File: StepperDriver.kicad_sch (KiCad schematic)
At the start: 13 parts, among them U5 A4988SETTR-T

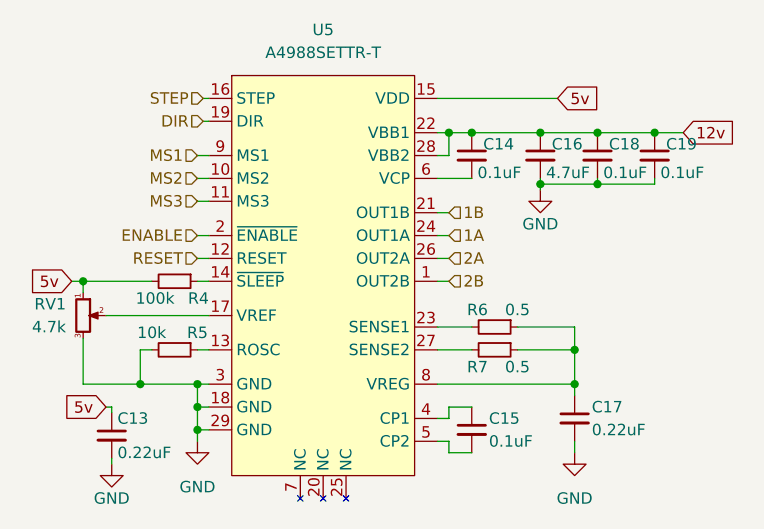
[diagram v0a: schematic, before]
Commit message: Added part numbers to majority of components
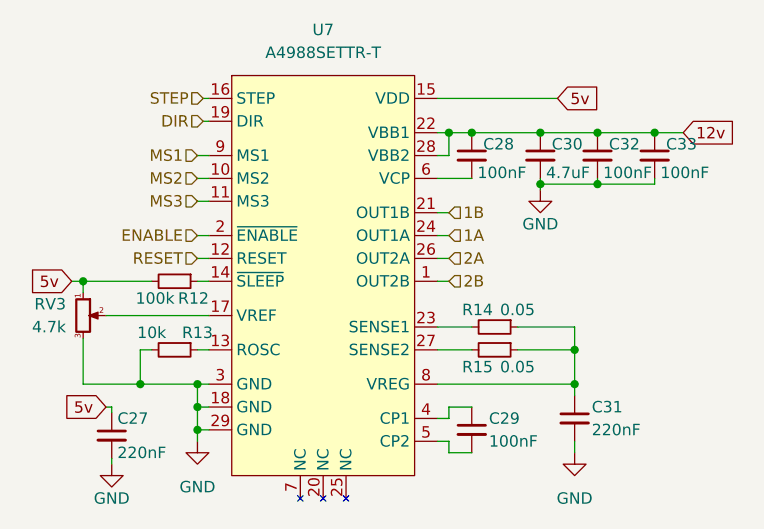
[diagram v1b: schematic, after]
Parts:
- C27: renamed from C13; value 0.22uF -> 220nF; footprint (none) -> Capacitor_SMD:C_0603_1608Metric; LSCS Part Number (none) -> C21120; Manufacturer Part Number (none) -> CL10B224KA8NNNC
- C28: renamed from C14; value 0.1uF -> 100nF; footprint (none) -> Capacitor_SMD:C_0603_1608Metric; LSCS Part Number (none) -> C1591; Manufacturer Part Number (none) -> CL10B104KB8NNNC
- C29: renamed from C15; value 0.1uF -> 100nF; footprint (none) -> Capacitor_SMD:C_0603_1608Metric; LSCS Part Number (none) -> C1591; Manufacturer Part Number (none) -> CL10B104KB8NNNC
- C30: renamed from C16; footprint (none) -> Capacitor_SMD:C_0603_1608Metric; LSCS Part Number (none) -> C69335; Manufacturer Part Number (none) -> CL10A475KA8NQNC
- C31: renamed from C17; value 0.22uF -> 220nF; footprint (none) -> Capacitor_SMD:C_0603_1608Metric; LSCS Part Number (none) -> C21120; Manufacturer Part Number (none) -> CL10B224KA8NNNC
- C32: renamed from C18; value 0.1uF -> 100nF; footprint (none) -> Capacitor_SMD:C_0603_1608Metric; LSCS Part Number (none) -> C1591; Manufacturer Part Number (none) -> CL10B104KB8NNNC
- C33: renamed from C19; value 0.1uF -> 100nF; footprint (none) -> Capacitor_SMD:C_0603_1608Metric; LSCS Part Number (none) -> C1591; Manufacturer Part Number (none) -> CL10B104KB8NNNC
- R12: renamed from R4; footprint (none) -> Resistor_SMD:R_0603_1608Metric; LSCS Part Number (none) -> C14675; Manufacturer Part Number (none) -> RC0603FR-07100KL
- R13: renamed from R5; footprint (none) -> Resistor_SMD:R_0603_1608Metric; LSCS Part Number (none) -> C25804; Manufacturer Part Number (none) -> 0603WAF1002T5E
- R14: renamed from R6; value 0.5 -> 0.05; footprint (none) -> Resistor_SMD:R_0603_1608Metric; LSCS Part Number (none) -> C158895; Manufacturer Part Number (none) -> RTT03R050FTP
- R15: renamed from R7; value 0.5 -> 0.05; footprint (none) -> Resistor_SMD:R_0603_1608Metric; LSCS Part Number (none) -> C158895; Manufacturer Part Number (none) -> RTT03R050FTP
- RV3: renamed from RV1; Manufacturer Part Number (none) -> VG039NCHXTB472
- U7: renamed from U5; Manufacturer Part Number (none) -> A4988SETTR-T

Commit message: Started assigning footprints
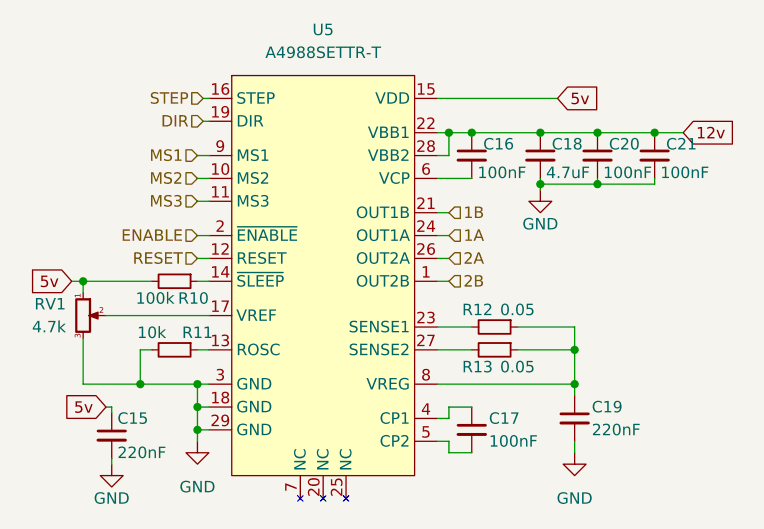
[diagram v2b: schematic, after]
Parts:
- U5: renamed from U7; footprint (none) -> Package_DFN_QFN:QFN-28-1EP_5x5mm_P0.5mm_EP3.35x3.35mm_ThermalVias
- renumbered C27 to C15, C28 to C16, C29 to C17, C30 to C18, C31 to C19, C32 to C20, C33 to C21, R12 to R10, R13 to R11, R14 to R12, R15 to R13, RV3 to RV1
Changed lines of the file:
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@@
   (symbol (lib_id "Device:R_Small") (at 159.385 97.79 270)
     (in_bom yes) (on_board yes)
-    (property "Reference" "R15" (id 0) (at 157.48 99.695 90))
+    (property "Reference" "R13" (id 0) (at 157.48 99.695 90))
     (property "Value" "0.05" (id 1) (at 161.925 99.695 90))
     (property "Footprint" "Resistor_SMD:R_0603_1608Metric" (id 2) (at 159.385 97.79 0)
@@
   (symbol (lib_id "Device:C_Small") (at 164.465 76.2 0)
     (in_bom yes) (on_board yes)
-    (property "Reference" "C30" (id 0) (at 165.735 74.9362 0)
+    (property "Reference" "C18" (id 0) (at 165.735 74.9362 0)
       (effects (font (size 1.27 1.27)) (justify left))
     )
@@
   (symbol (lib_id "power:GND") (at 168.275 109.22 0)
     (in_bom yes) (on_board yes) (fields_autoplaced)
-    (property "Reference" "#PWR021" (id 0) (at 168.275 115.57 0)
+    (property "Reference" "#PWR025" (id 0) (at 168.275 115.57 0)
       (effects (font (size 1.27 1.27)) hide)
     )
@@
   (symbol (lib_id "Device:R_Potentiometer_Small") (at 113.665 93.98 0)
     (in_bom yes) (on_board yes)
-    (property "Reference" "RV3" (id 0) (at 111.76 92.7099 0)
+    (property "Reference" "RV1" (id 0) (at 111.76 92.7099 0)
       (effects (font (size 1.27 1.27)) (justify right))
     )
@@
   (symbol (lib_id "Device:C_Small") (at 116.84 107.315 0)
     (in_bom yes) (on_board yes)
-    (property "Reference" "C27" (id 0) (at 117.475 105.4162 0)
+    (property "Reference" "C15" (id 0) (at 117.475 105.4162 0)
       (effects (font (size 1.27 1.27)) (justify left))
     )
@@
   (symbol (lib_id "power:GND") (at 116.84 110.49 0)
     (in_bom yes) (on_board yes)
-    (property "Reference" "#PWR018" (id 0) (at 116.84 116.84 0)
+    (property "Reference" "#PWR022" (id 0) (at 116.84 116.84 0)
       (effects (font (size 1.27 1.27)) hide)
     )
@@
   (symbol (lib_name "A4988SETTR-T_1") (lib_id "MotorBoard:A4988SETTR-T") (at 130.175 67.31 0)
     (in_bom yes) (on_board yes) (fields_autoplaced)
-    (property "Reference" "U7" (id 0) (at 140.335 62.23 0))
+    (property "Reference" "U5" (id 0) (at 140.335 62.23 0))
     (property "Value" "A4988SETTR-T" (id 1) (at 140.335 64.77 0))
-    (property "Footprint" "" (id 2) (at 165.735 68.58 0)
+    (property "Footprint" "Package_DFN_QFN:QFN-28-1EP_5x5mm_P0.5mm_EP3.35x3.35mm_ThermalVias" (id 2) (at 165.735 68.58 0)
       (effects (font (size 1.27 1.27)) hide)
     )
@@
   (symbol (lib_id "Device:C_Small") (at 156.845 76.2 0)
     (in_bom yes) (on_board yes)
-    (property "Reference" "C28" (id 0) (at 158.115 74.9362 0)
+    (property "Reference" "C16" (id 0) (at 158.115 74.9362 0)
       (effects (font (size 1.27 1.27)) (justify left))
     )
@@
   (symbol (lib_id "Device:R_Small") (at 159.385 95.25 270)
     (in_bom yes) (on_board yes)
-    (property "Reference" "R14" (id 0) (at 157.48 93.345 90))
+    (property "Reference" "R12" (id 0) (at 157.48 93.345 90))
     (property "Value" "0.05" (id 1) (at 161.925 93.345 90))
     (property "Footprint" "Resistor_SMD:R_0603_1608Metric" (id 2) (at 159.385 95.25 0)
@@
   (symbol (lib_id "Device:R_Small") (at 123.825 90.17 270)
     (in_bom yes) (on_board yes)
-    (property "Reference" "R12" (id 0) (at 127.6349 92.075 90)
+    (property "Reference" "R10" (id 0) (at 127.6349 92.075 90)
       (effects (font (size 1.27 1.27)) (justify right))
     )
@@
   (symbol (lib_id "Device:C_Small") (at 170.815 76.2 0)
     (in_bom yes) (on_board yes)
-    (property "Reference" "C32" (id 0) (at 172.085 74.9362 0)
+    (property "Reference" "C20" (id 0) (at 172.085 74.9362 0)
       (effects (font (size 1.27 1.27)) (justify left))
     )
@@
   (symbol (lib_id "Device:C_Small") (at 177.165 76.2 0)
     (in_bom yes) (on_board yes)
-    (property "Reference" "C33" (id 0) (at 178.435 74.9362 0)
+    (property "Reference" "C21" (id 0) (at 178.435 74.9362 0)
       (effects (font (size 1.27 1.27)) (justify left))
     )
@@
   (symbol (lib_id "Device:C_Small") (at 168.275 105.41 0)
     (in_bom yes) (on_board yes)
-    (property "Reference" "C31" (id 0) (at 170.18 104.1462 0)
+    (property "Reference" "C19" (id 0) (at 170.18 104.1462 0)
       (effects (font (size 1.27 1.27)) (justify left))
     )
@@
   (symbol (lib_id "power:GND") (at 164.465 80.01 0)
     (in_bom yes) (on_board yes)
-    (property "Reference" "#PWR020" (id 0) (at 164.465 86.36 0)
+    (property "Reference" "#PWR024" (id 0) (at 164.465 86.36 0)
       (effects (font (size 1.27 1.27)) hide)
     )
@@
   (symbol (lib_id "Device:C_Small") (at 156.845 106.68 0)
     (in_bom yes) (on_board yes)
-    (property "Reference" "C29" (id 0) (at 158.75 105.4162 0)
+    (property "Reference" "C17" (id 0) (at 158.75 105.4162 0)
       (effects (font (size 1.27 1.27)) (justify left))
     )
@@
   (symbol (lib_id "Device:R_Small") (at 123.825 97.79 270)
     (in_bom yes) (on_board yes)
-    (property "Reference" "R13" (id 0) (at 126.365 95.885 90))
+    (property "Reference" "R11" (id 0) (at 126.365 95.885 90))
     (property "Value" "10k" (id 1) (at 121.285 95.885 90))
     (property "Footprint" "Resistor_SMD:R_0603_1608Metric" (id 2) (at 123.825 97.79 0)
@@
   (symbol (lib_id "power:GND") (at 126.365 107.95 0)
     (in_bom yes) (on_board yes) (fields_autoplaced)
-    (property "Reference" "#PWR019" (id 0) (at 126.365 114.3 0)
-      (effects (font (size 1.27 1.27)) hide)
-    )
+    (property "Reference" "#PWR023" (id 0) (at 126.365 114.3 0)
+      (effects (font (size 1.27 1.27)) hide)
+    )

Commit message: Added servo headers
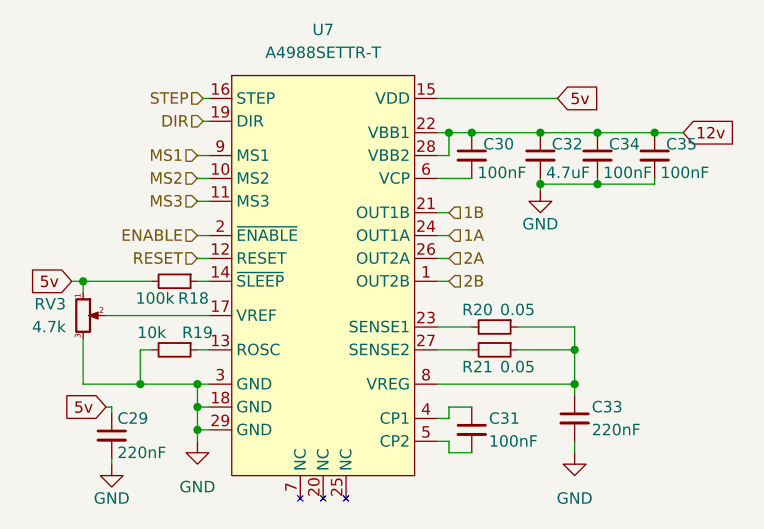
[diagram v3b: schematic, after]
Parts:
- RV3: renamed from RV1; footprint (none) -> MotorBoard:VG039NCHXTB472
- renumbered C15 to C29, C16 to C30, C17 to C31, C18 to C32, C19 to C33, C20 to C34, C21 to C35, R10 to R18, R11 to R19, R12 to R20, R13 to R21, U5 to U7
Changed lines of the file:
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@@
   (symbol (lib_id "Device:R_Small") (at 159.385 97.79 270)
     (in_bom yes) (on_board yes)
-    (property "Reference" "R13" (id 0) (at 157.48 99.695 90))
+    (property "Reference" "R21" (id 0) (at 157.48 99.695 90))
     (property "Value" "0.05" (id 1) (at 161.925 99.695 90))
     (property "Footprint" "Resistor_SMD:R_0603_1608Metric" (id 2) (at 159.385 97.79 0)
@@
   (symbol (lib_id "Device:C_Small") (at 164.465 76.2 0)
     (in_bom yes) (on_board yes)
-    (property "Reference" "C18" (id 0) (at 165.735 74.9362 0)
+    (property "Reference" "C32" (id 0) (at 165.735 74.9362 0)
       (effects (font (size 1.27 1.27)) (justify left))
     )
@@
   (symbol (lib_id "power:GND") (at 168.275 109.22 0)
     (in_bom yes) (on_board yes) (fields_autoplaced)
-    (property "Reference" "#PWR025" (id 0) (at 168.275 115.57 0)
+    (property "Reference" "#PWR033" (id 0) (at 168.275 115.57 0)
       (effects (font (size 1.27 1.27)) hide)
     )
@@
   (symbol (lib_id "Device:R_Potentiometer_Small") (at 113.665 93.98 0)
     (in_bom yes) (on_board yes)
-    (property "Reference" "RV1" (id 0) (at 111.76 92.7099 0)
+    (property "Reference" "RV3" (id 0) (at 111.76 92.7099 0)
       (effects (font (size 1.27 1.27)) (justify right))
     )
@@
       (effects (font (size 1.27 1.27)) (justify right))
     )
-    (property "Footprint" "" (id 2) (at 113.665 93.98 0)
+    (property "Footprint" "MotorBoard:VG039NCHXTB472" (id 2) (at 113.665 93.98 0)
       (effects (font (size 1.27 1.27)) hide)
     )
@@
   (symbol (lib_id "Device:C_Small") (at 116.84 107.315 0)
     (in_bom yes) (on_board yes)
-    (property "Reference" "C15" (id 0) (at 117.475 105.4162 0)
+    (property "Reference" "C29" (id 0) (at 117.475 105.4162 0)
       (effects (font (size 1.27 1.27)) (justify left))
     )
@@
   (symbol (lib_id "power:GND") (at 116.84 110.49 0)
     (in_bom yes) (on_board yes)
-    (property "Reference" "#PWR022" (id 0) (at 116.84 116.84 0)
+    (property "Reference" "#PWR030" (id 0) (at 116.84 116.84 0)
       (effects (font (size 1.27 1.27)) hide)
     )
@@
   (symbol (lib_name "A4988SETTR-T_1") (lib_id "MotorBoard:A4988SETTR-T") (at 130.175 67.31 0)
     (in_bom yes) (on_board yes) (fields_autoplaced)
-    (property "Reference" "U5" (id 0) (at 140.335 62.23 0))
+    (property "Reference" "U7" (id 0) (at 140.335 62.23 0))
     (property "Value" "A4988SETTR-T" (id 1) (at 140.335 64.77 0))
     (property "Footprint" "Package_DFN_QFN:QFN-28-1EP_5x5mm_P0.5mm_EP3.35x3.35mm_ThermalVias" (id 2) (at 165.735 68.58 0)
@@
   (symbol (lib_id "Device:C_Small") (at 156.845 76.2 0)
     (in_bom yes) (on_board yes)
-    (property "Reference" "C16" (id 0) (at 158.115 74.9362 0)
+    (property "Reference" "C30" (id 0) (at 158.115 74.9362 0)
       (effects (font (size 1.27 1.27)) (justify left))
     )
@@
   (symbol (lib_id "Device:R_Small") (at 159.385 95.25 270)
     (in_bom yes) (on_board yes)
-    (property "Reference" "R12" (id 0) (at 157.48 93.345 90))
+    (property "Reference" "R20" (id 0) (at 157.48 93.345 90))
     (property "Value" "0.05" (id 1) (at 161.925 93.345 90))
     (property "Footprint" "Resistor_SMD:R_0603_1608Metric" (id 2) (at 159.385 95.25 0)
@@
   (symbol (lib_id "Device:R_Small") (at 123.825 90.17 270)
     (in_bom yes) (on_board yes)
-    (property "Reference" "R10" (id 0) (at 127.6349 92.075 90)
+    (property "Reference" "R18" (id 0) (at 127.6349 92.075 90)
       (effects (font (size 1.27 1.27)) (justify right))
     )
@@
   (symbol (lib_id "Device:C_Small") (at 170.815 76.2 0)
     (in_bom yes) (on_board yes)
-    (property "Reference" "C20" (id 0) (at 172.085 74.9362 0)
+    (property "Reference" "C34" (id 0) (at 172.085 74.9362 0)
       (effects (font (size 1.27 1.27)) (justify left))
     )
@@
   (symbol (lib_id "Device:C_Small") (at 177.165 76.2 0)
     (in_bom yes) (on_board yes)
-    (property "Reference" "C21" (id 0) (at 178.435 74.9362 0)
+    (property "Reference" "C35" (id 0) (at 178.435 74.9362 0)
       (effects (font (size 1.27 1.27)) (justify left))
     )
@@
   (symbol (lib_id "Device:C_Small") (at 168.275 105.41 0)
     (in_bom yes) (on_board yes)
-    (property "Reference" "C19" (id 0) (at 170.18 104.1462 0)
+    (property "Reference" "C33" (id 0) (at 170.18 104.1462 0)
       (effects (font (size 1.27 1.27)) (justify left))
     )
@@
   (symbol (lib_id "power:GND") (at 164.465 80.01 0)
     (in_bom yes) (on_board yes)
-    (property "Reference" "#PWR024" (id 0) (at 164.465 86.36 0)
+    (property "Reference" "#PWR032" (id 0) (at 164.465 86.36 0)
       (effects (font (size 1.27 1.27)) hide)
     )
@@
   (symbol (lib_id "Device:C_Small") (at 156.845 106.68 0)
     (in_bom yes) (on_board yes)
-    (property "Reference" "C17" (id 0) (at 158.75 105.4162 0)
+    (property "Reference" "C31" (id 0) (at 158.75 105.4162 0)
       (effects (font (size 1.27 1.27)) (justify left))
     )
@@
   (symbol (lib_id "Device:R_Small") (at 123.825 97.79 270)
     (in_bom yes) (on_board yes)
-    (property "Reference" "R11" (id 0) (at 126.365 95.885 90))
+    (property "Reference" "R19" (id 0) (at 126.365 95.885 90))
     (property "Value" "10k" (id 1) (at 121.285 95.885 90))
     (property "Footprint" "Resistor_SMD:R_0603_1608Metric" (id 2) (at 123.825 97.79 0)
@@
   (symbol (lib_id "power:GND") (at 126.365 107.95 0)
     (in_bom yes) (on_board yes) (fields_autoplaced)
-    (property "Reference" "#PWR023" (id 0) (at 126.365 114.3 0)
-      (effects (font (size 1.27 1.27)) hide)
-    )
+    (property "Reference" "#PWR031" (id 0) (at 126.365 114.3 0)
+      (effects (font (size 1.27 1.27)) hide)
+    )

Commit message: Began work on PCB layout
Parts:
- removed C33: 220nF, Capacitor_SMD:C_0603_1608Metric, symbol Device:C_Small
- added C19: 220nF, Capacitor_SMD:C_0603_1608Metric, symbol Device:C_Small
- renumbered C29 to C15, C30 to C16, C31 to C17, C32 to C18, C34 to C20, C35 to C21, R18 to R10, R19 to R11, R20 to R12, R21 to R13, RV3 to RV1, U7 to U5
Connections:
- net GND: now also R12.1, R13.1, C19.2
- new net: C19.1, U5.8 (VREG)
